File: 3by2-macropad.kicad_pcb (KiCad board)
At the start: 2 copper layers, 65.1 x 77.8 mm, 13 parts, among them U1 Pico

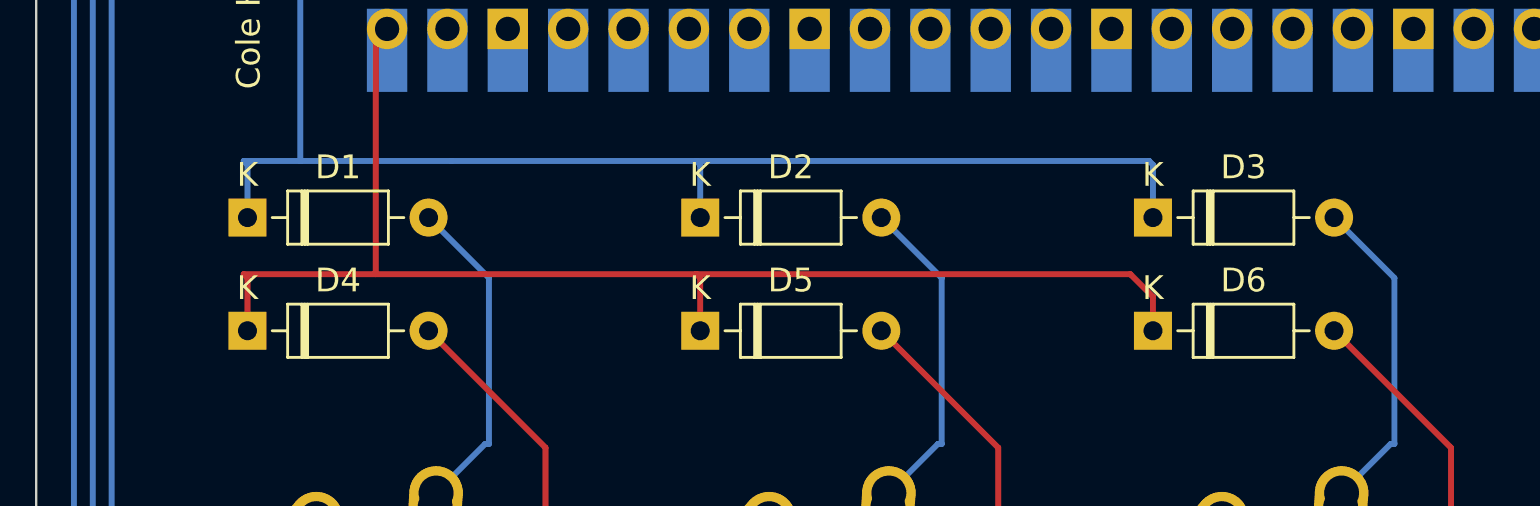
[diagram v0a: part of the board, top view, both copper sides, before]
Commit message: Used correct diode
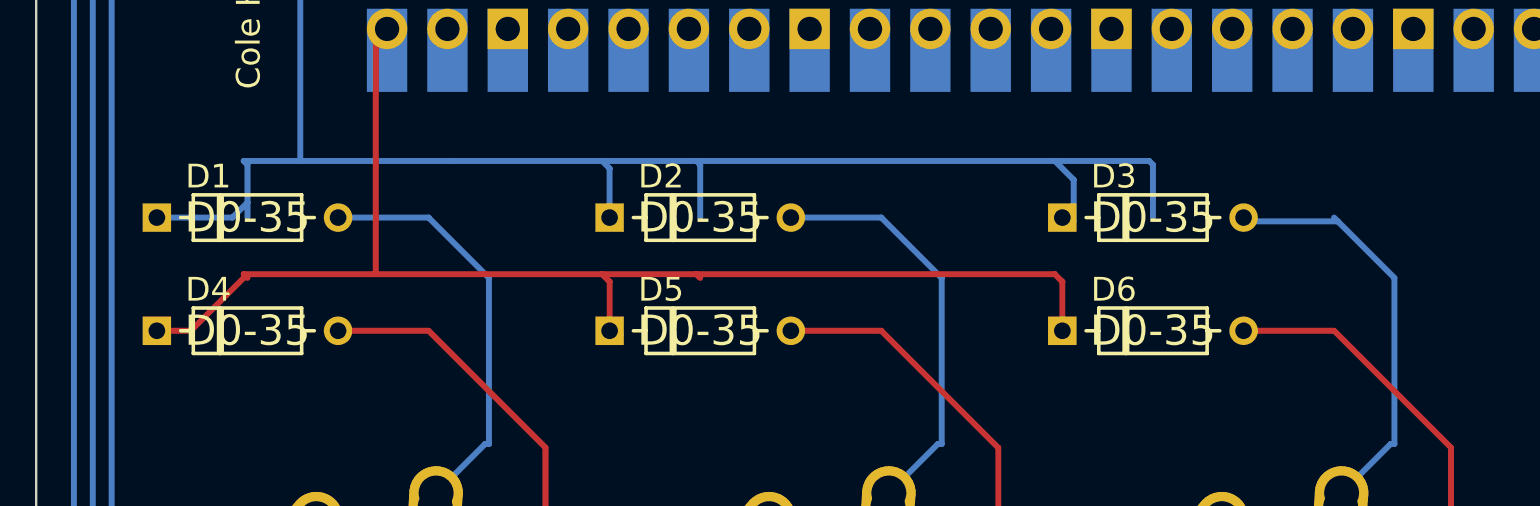
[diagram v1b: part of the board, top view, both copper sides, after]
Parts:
- D1, D2, D3, D4, D5, D6: footprint Diode_THT:D_DO-35_SOD27_P7.62mm_Horizontal -> onesemi-1N914:ON_Semiconductor-017AG-08_2016-O-MFG
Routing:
- net ROW0: track 70.3 -> 80.3 mm
- net Net-(D3-A): track 13.7 -> 18.0 mm
- net Net-(D6-A): track 29.9 -> 33.7 mm
- net Net-(D4-A): track 30.4 -> 34.2 mm
- net Net-(D1-A): track 13.7 -> 17.5 mm
- net Net-(D5-A): track 29.9 -> 33.7 mm
- net Net-(D2-A): track 13.7 -> 17.5 mm
